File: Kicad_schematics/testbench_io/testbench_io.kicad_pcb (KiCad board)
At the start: 2 copper layers, 182.6 x 130 mm, 73 parts, among them J101 Conn_01x02, J102 Conn_01x02, J103 Conn_01x02, J104 DB37_Female_MountingHoles, J301 Conn_01x12, Q201 2N3904, Q301 IPD50R380CE, Q302 IPD50R380CE, Q303 IPD50R380CE, Q304 IPD50R380CE, Q305 IPD50R380CE, Q306 IPD50R380CE, SW101 SW_SPST, SW102 SW_Push, SW103 SW_Push, SW104 SW_Push, SW105 SW_Push, SW106 SW_SPST, SW107 SW_SPST, SW108 SW_DIP_x08, SW109 SW_SPST, SW110 SW_Push, SW111 SW_SPST, SW112 SW_SPST, SW113 SW_SPST, SW114 SW_DPDT_x2, SW201 SW_DIP_x01, U101 NUCLEO64-F476RG, U102 CJMCU_MCP2551, U201 PCF8574AN

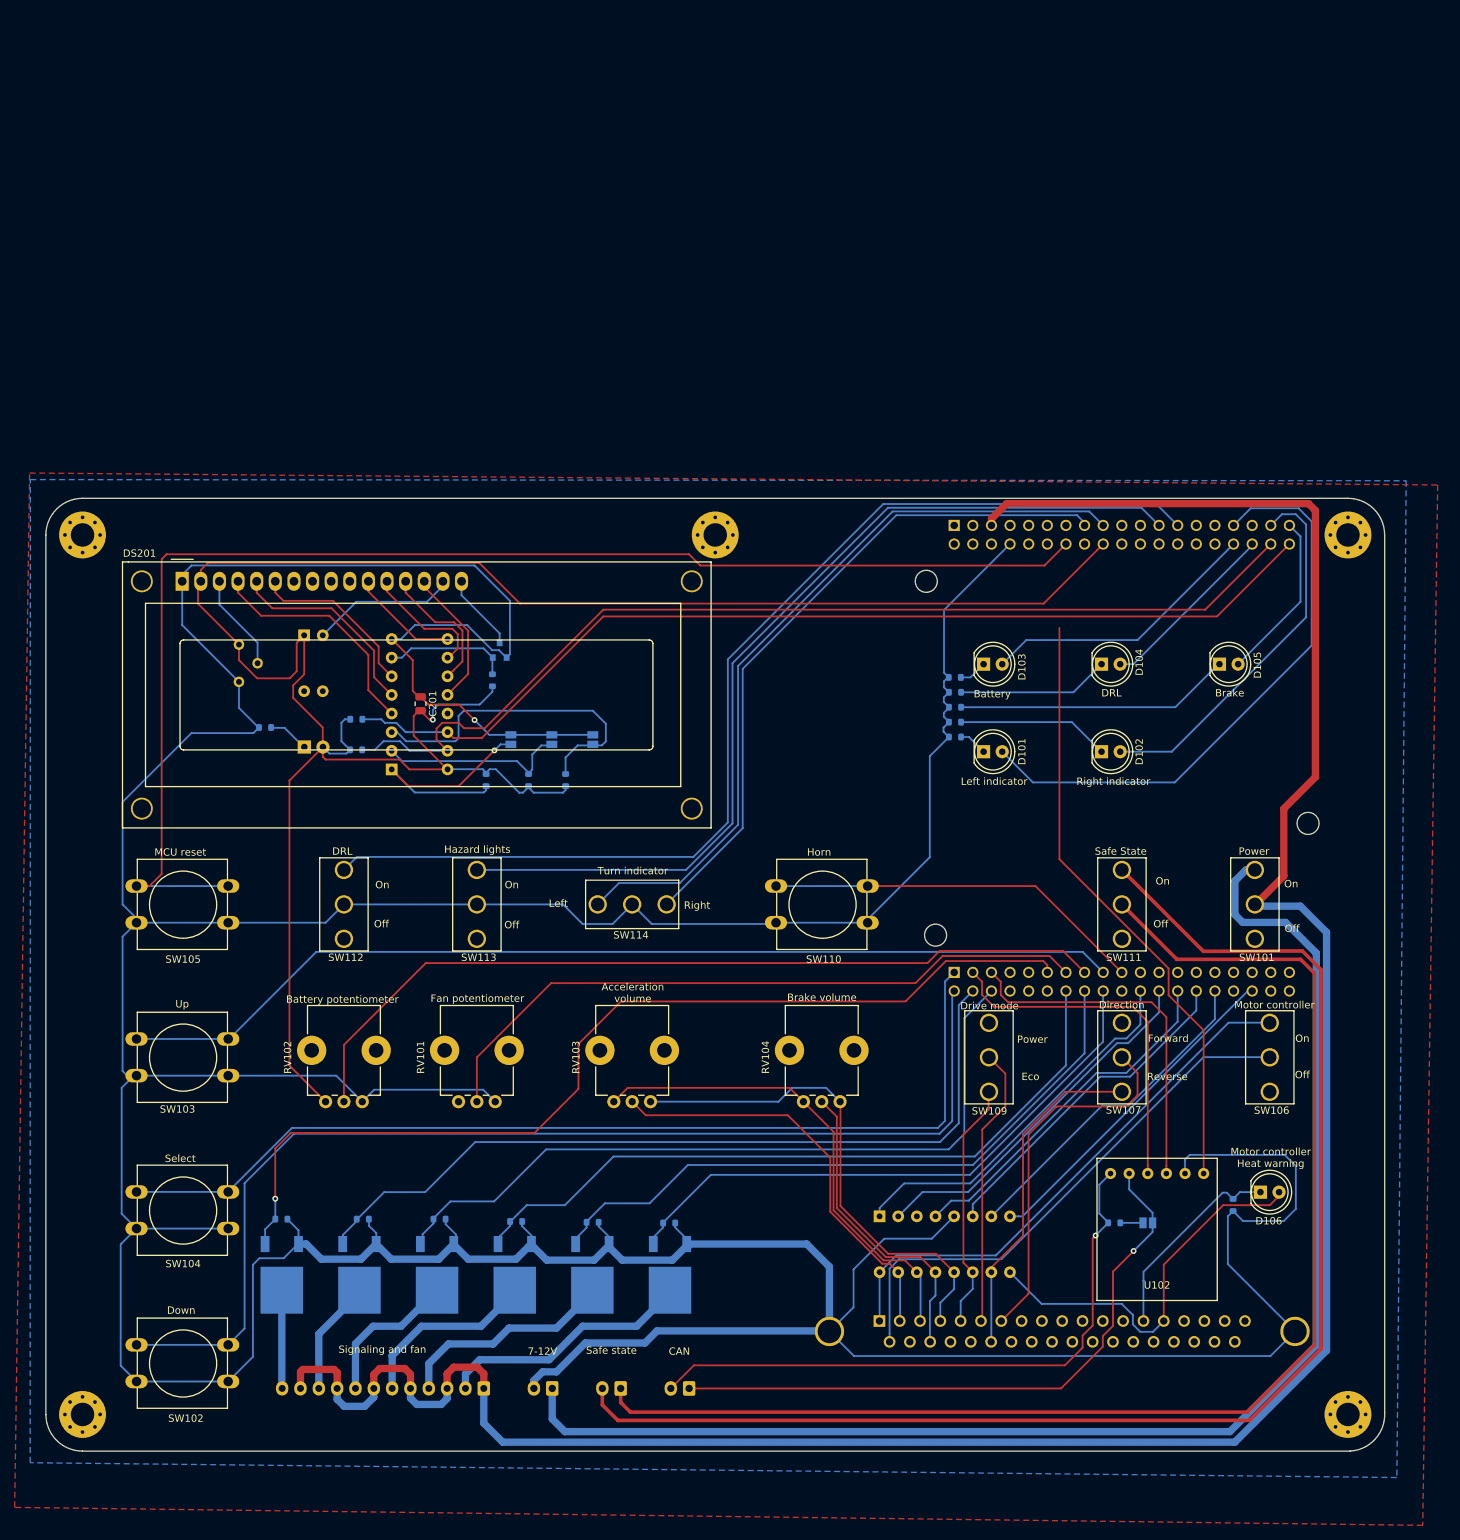
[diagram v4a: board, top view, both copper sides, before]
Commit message: Fixed some footprints
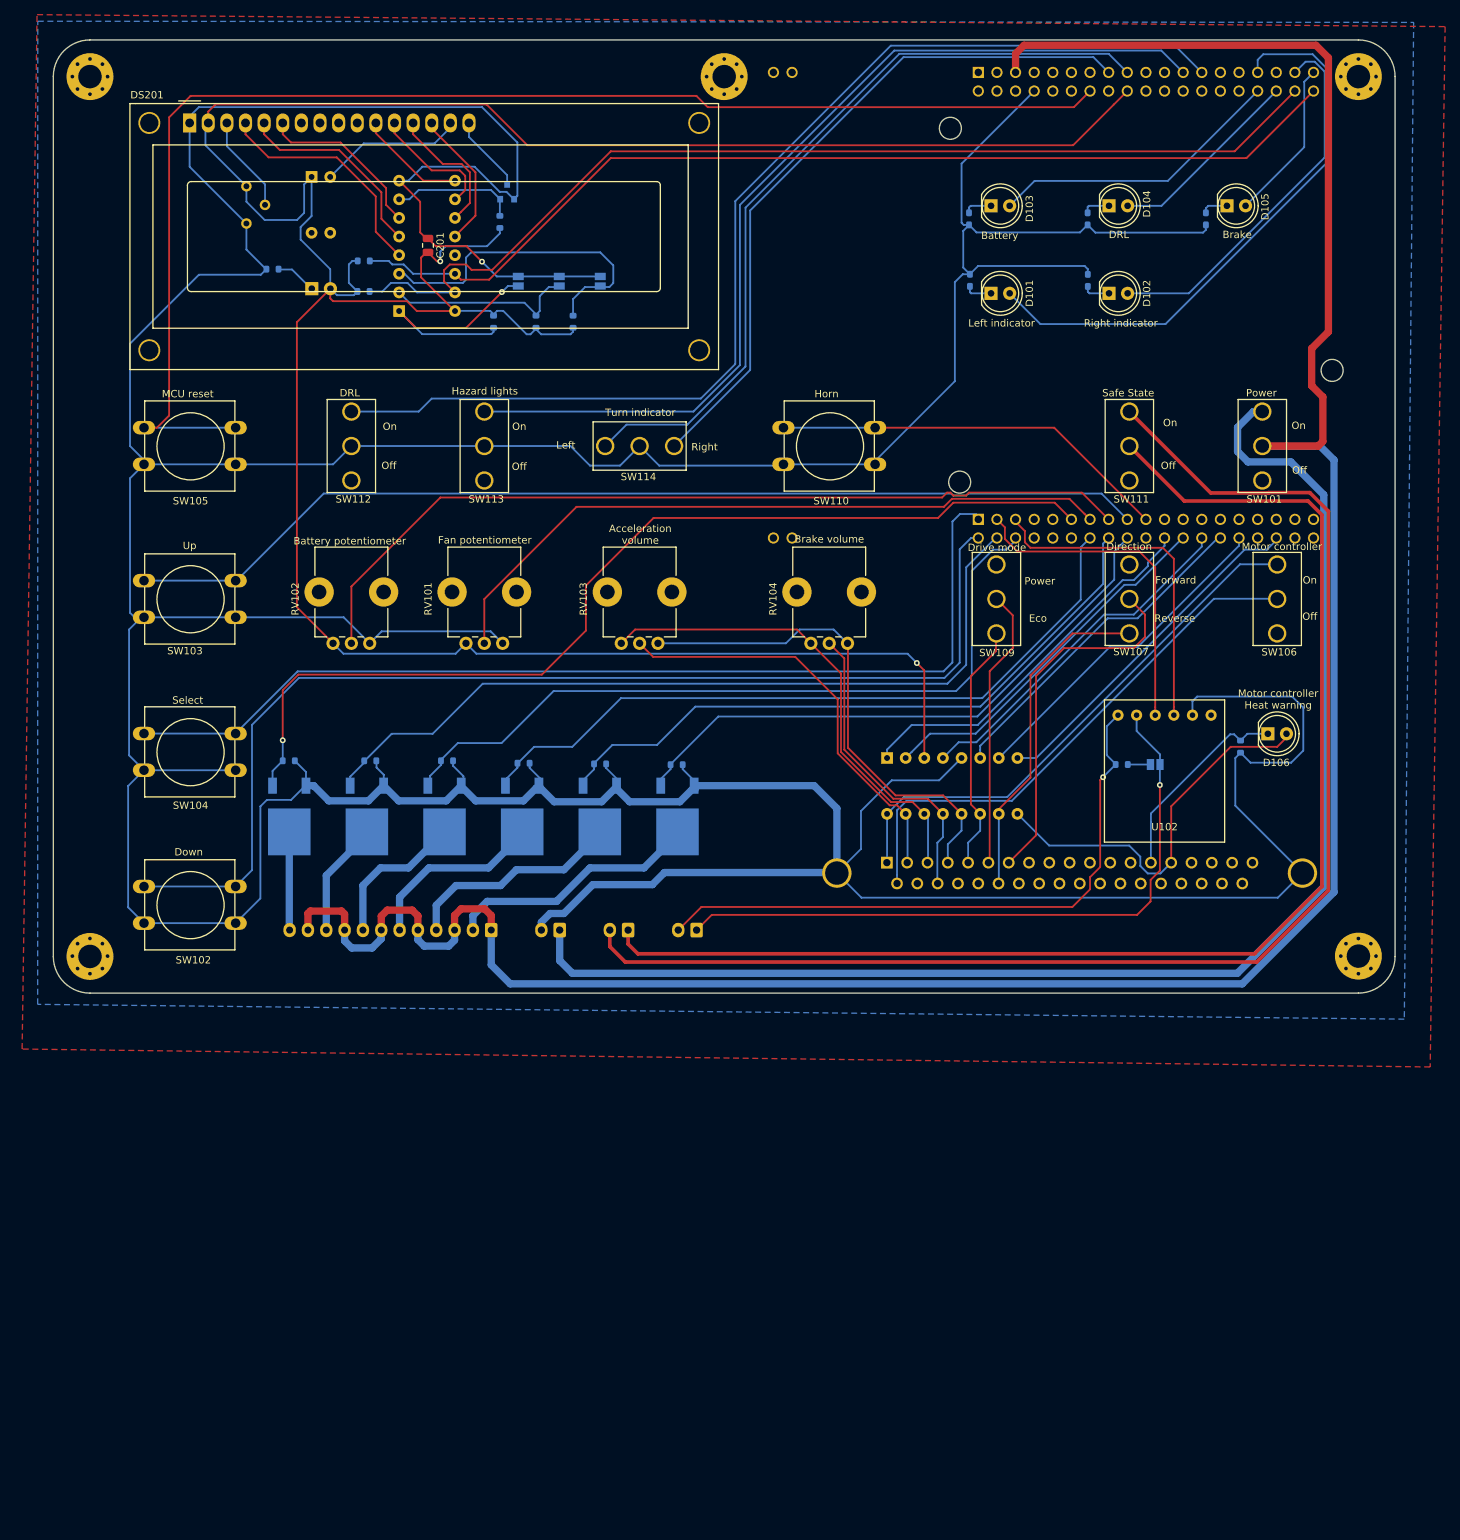
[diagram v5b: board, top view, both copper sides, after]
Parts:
- moved R106 74.9 mm to (177.6, 44.8), turned to 270 degrees
- moved R105 67.1 mm to (161.5, 44.8), turned to 270 degrees
- moved R102 62.9 mm to (161.5, 53.2), turned to 90 degrees
- moved R103 62.6 mm to (145.3, 44.8), turned to 270 degrees
- moved H105 62.5 mm to (198.4, 25.4)
- moved H104 62.5 mm to (198.4, 145.4)
- moved H101 62.5 mm to (111.9, 25.4)
- moved J104 62.5 mm to (134.1, 132.6)
- moved R301 62.5 mm to (105.4, 119.2)
- moved R304 62.5 mm to (74.1, 118.7)
- moved R305 62.5 mm to (63.6, 118.7)
- moved R306 62.5 mm to (52.5, 118.7)
- moved SW108 62.5 mm to (134.1, 118.3)
- moved D103 62.5 mm to (148.3, 43.0)
- moved D104 62.5 mm to (164.4, 43.0)
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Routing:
- net GND: track 816.5 -> 868.3 mm
- net Net-(D105-Pad1): track 37.7 -> 3.63 mm
- net Net-(D102-Pad1): track 20.8 -> 3.69 mm
- net Net-(D104-Pad1): track 20.8 -> 3.78 mm
- net MCU_5V: track 383.6 -> 398.3 mm, vias 1 -> 2
- net VDD_MCU: track 343.8 -> 350.2 mm
- net Net-(J102-Pad1): track 86.5 -> 90.8 mm
- net /CRX: track 48.4 -> 45.4 mm
- net /Battery_pot: track 115.3 -> 118.2 mm
- net /Up: track 139.2 -> 142.0 mm
- net /Horn_sw: track 52.0 -> 54.6 mm
- net /DRL_sw: track 148.6 -> 151.2 mm
- net /CTX: track 48.8 -> 46.2 mm
- net /Left_sw: track 104.6 -> 107.1 mm
- net /HL_sw: track 127.3 -> 129.7 mm
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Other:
- board size 182.6 x 130 mm -> 183 x 130 mm
- board text removed: "7-12V"
- board text removed: "CAN"
- board text removed: "Safe state"
- board text removed: "Signaling and fan"

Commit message: Fixed some final stuff
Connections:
- U101 pad 19: Net-(U101-Pad19) -> GND
- U101 pad 20: Net-(U101-Pad20) -> GND
- U101 pad 22: Net-(U101-Pad22) -> GND
- U101 pad 24: Net-(U101-Pad24) -> VDD_MCU
- U101 pad 31: /Left_LED -> Net-(U101-Pad31)
- U101 pad 35: /Right_LED -> Net-(U101-Pad35)
- U101 pad 37: /Brake_LED -> Net-(U101-Pad37)
- U101 pad 47: Net-(U101-Pad47) -> GND
- U101 pad 5: VDD_MCU -> Net-(U101-Pad5)
- U101 pad 58: Net-(U101-Pad58) -> GND
- U101 pad 61: Net-(U101-Pad61) -> /Left_LED
- U101 pad 63: Net-(U101-Pad63) -> /Right_LED
- U101 pad 65: Net-(U101-Pad65) -> /Brake_LED
- U101 pad 77: Net-(U101-Pad77) -> GND
- U101 pad 78: Net-(U101-Pad78) -> GND
- U101 pad 79: Net-(U101-Pad79) -> GND
- U101 pad 80: Net-(U101-Pad80) -> GND
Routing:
- net /Left_LED: track 79.6 -> 44.1 mm
- net VDD_MCU: track 350.2 -> 314.9 mm
- net /Brake_LED: track 22.0 -> 44.2 mm
- net Net-(J101-Pad2): track 189.7 -> 207.4 mm
- net /Right_LED: track 51.5 -> 35.3 mm
- net Net-(J101-Pad1): track 181.7 -> 195.2 mm
- net V_external: track 189.3 -> 198.7 mm
- net /CRX: track 45.4 -> 43.5 mm
- net /CTX: track 46.2 -> 44.4 mm
- net /Select: track 137.2 -> 135.4 mm
- net /Right_acti: track 99.0 -> 97.8 mm
- net /Battery_pot: track 118.2 -> 117.3 mm
- net /Left_acti: track 90.2 -> 89.4 mm
- net /Up: track 142.0 -> 141.2 mm
- net /Acc_vol: track 50.3 -> 51.0 mm
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
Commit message: Made the power planes nicer.
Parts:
- moved R305 0.50 mm to (63.1, 118.7)
- moved R303 0.25 mm to (84.3, 119.0)
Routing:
- net MCU_5V: track 398.3 -> 176.4 mm, vias 2 -> 1
- net GND: track 868.3 -> 803.9 mm, vias 1 -> 0
- net /Reset: track 185.7 -> 199.0 mm
- net /Select: track 135.4 -> 130.1 mm
- net /Down: track 154.2 -> 148.9 mm
- net /SDA: track 143.1 -> 138.6 mm
- net Net-(J102-Pad1): track 90.8 -> 86.8 mm
- net /Battery_LED: track 40.3 -> 44.2 mm
- net /Fan_pwm: track 111.4 -> 108.8 mm
- net Net-(JP203-Pad1): track 45.0 -> 42.6 mm, vias 0 -> 2
- net VDD_MCU: track 314.9 -> 313.3 mm
- net Net-(JP201-Pad1): track 34.5 -> 32.9 mm, vias 1 -> 2
- net V_external: track 198.7 -> 197.4 mm
- net /Front_acti: track 104.3 -> 103.0 mm
- net /SCL: track 140.6 -> 139.8 mm
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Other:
- board text added: "120R jumper"

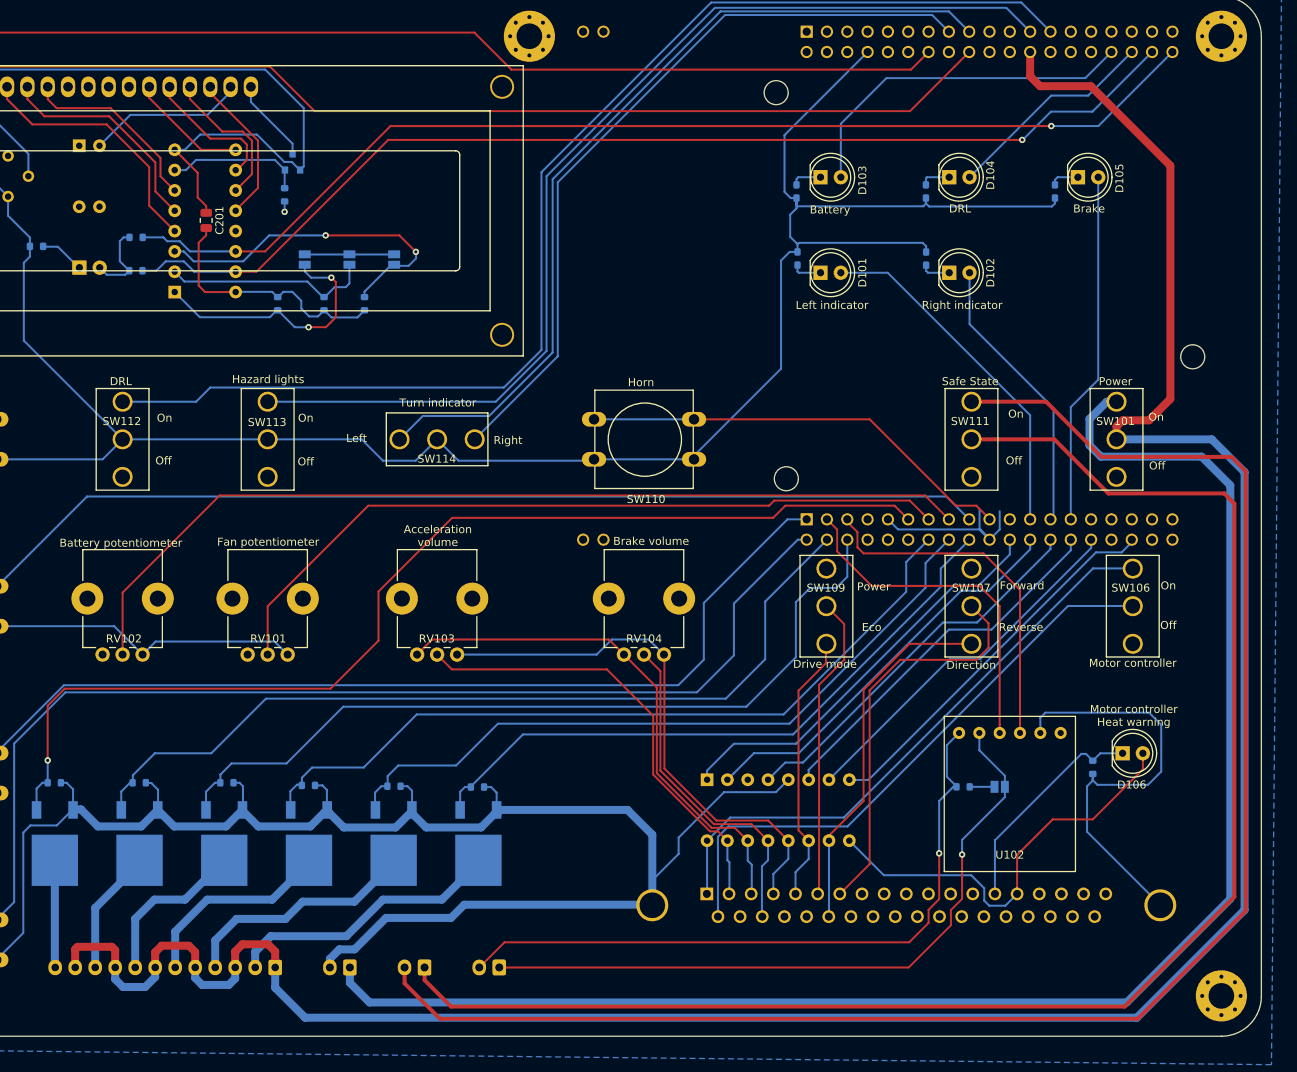
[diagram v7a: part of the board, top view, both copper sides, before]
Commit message: Change of connector
Changed a connector that wasn't available
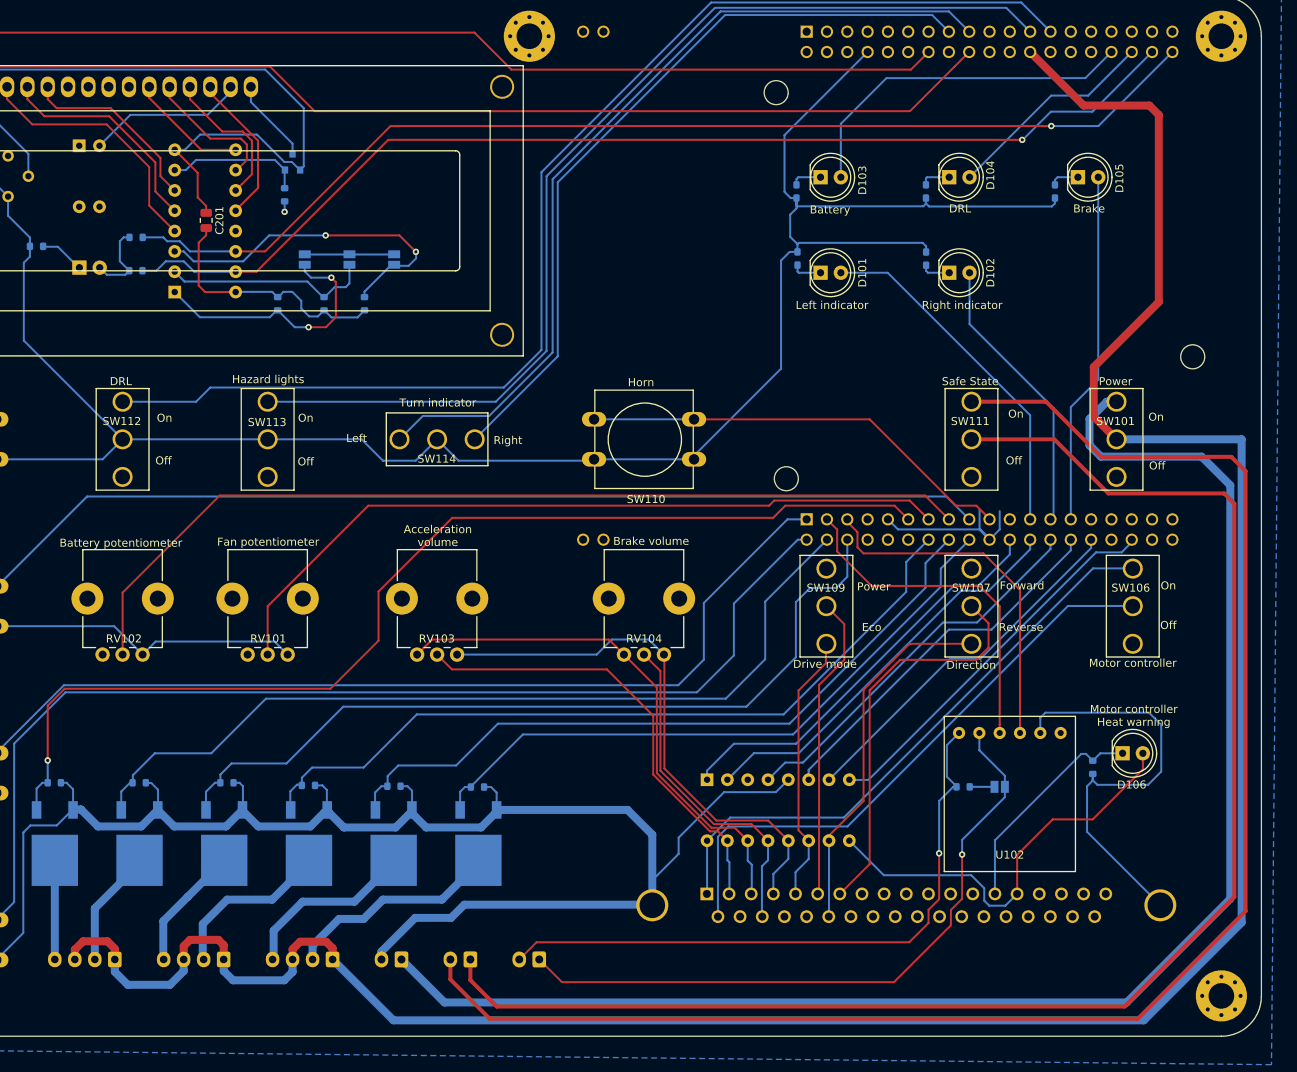
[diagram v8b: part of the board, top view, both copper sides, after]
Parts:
- added J302: Conn_01x04, Connector_JST:JST_XH_S4B-XH-A_1x04_P2.50mm_Horizontal, B.Cu at (73.7, 140.8)
- added J303: Conn_01x04, Connector_JST:JST_XH_S4B-XH-A_1x04_P2.50mm_Horizontal, B.Cu at (87.3, 140.8)
- J101, J102, J103: footprint Connector_JST:JST_XH_S2B-XH-A-1_1x02_P2.50mm_Horizontal -> Connector_JST:JST_XH_S2B-XH-A_1x02_P2.50mm_Horizontal
- J301: value Conn_01x12 -> Conn_01x04; footprint Connector_JST:JST_XH_S12B-XH-A-1_1x12_P2.50mm_Horizontal -> Connector_JST:JST_XH_S4B-XH-A_1x04_P2.50mm_Horizontal
- moved J301 20.1 mm to (60.1, 140.8)
- moved J103 6.53 mm to (95.9, 140.8)
- moved J101 5.81 mm to (104.5, 140.8)
- moved J102 5.10 mm to (113.1, 140.8)
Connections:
- J301 pad 2: /Solar_lights/Brake_lights_VSS -> /Solar_lights/Fan_VSS
- J301 pad 4: /Solar_lights/Left_indicator_VSS -> /Solar_lights/Horn_VSS
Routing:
- net /Solar_lights/Brake_lights_VSS: track 34.8 -> 27.1 mm
- net /Solar_lights/Left_indicator_VSS: track 30.0 -> 22.5 mm
- net V_external: track 197.4 -> 190.1 mm
- net GND: track 803.9 -> 797.0 mm
- net Net-(J102-Pad2): track 85.0 -> 79.6 mm
- net Net-(J101-Pad2): track 207.4 -> 202.3 mm
- net Net-(J101-Pad1): track 195.2 -> 190.5 mm
- net /Solar_lights/Front_lights_VSS: track 23.3 -> 18.6 mm
- net /Solar_lights/Right_indicator_VSS: track 25.1 -> 21.2 mm
- net Net-(J102-Pad1): track 86.8 -> 83.7 mm
- net /Solar_lights/Horn_VSS: track 13.4 -> 12.4 mm
- net /Solar_lights/Fan_VSS: track 16.3 -> 15.3 mm
